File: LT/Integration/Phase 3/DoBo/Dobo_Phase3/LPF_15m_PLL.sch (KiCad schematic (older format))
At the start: 11 parts, among them J300 Conn_Coaxial, J301 Conn_Coaxial

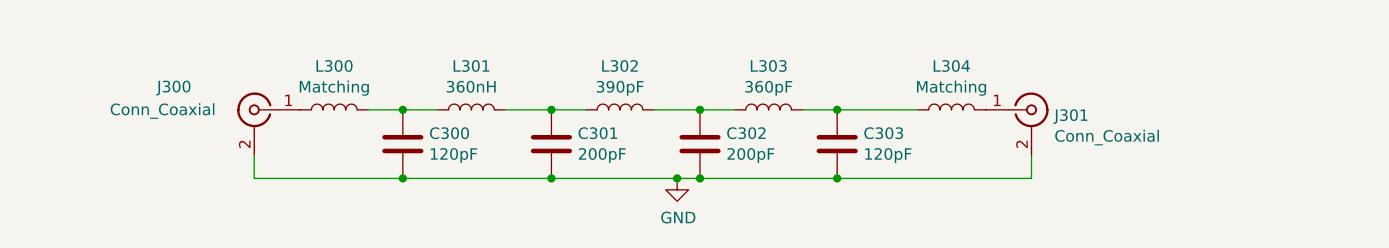
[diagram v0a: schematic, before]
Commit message: Added the completed layout for the DoBo Phase 3
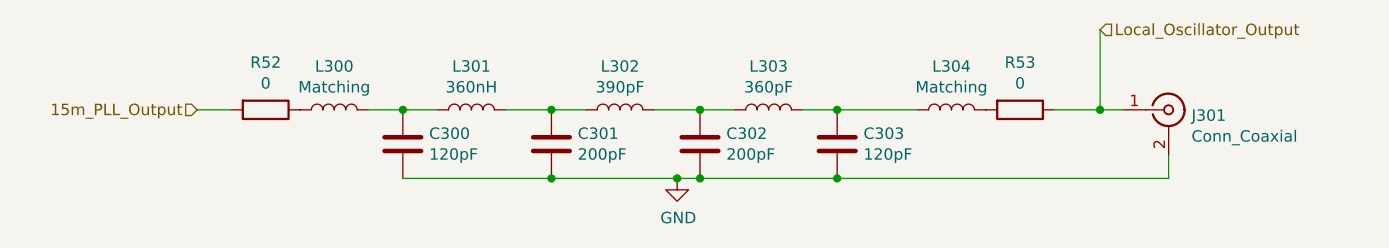
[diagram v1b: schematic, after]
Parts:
- removed J300: Conn_Coaxial, Connector_Coaxial:SMA_Amphenol_132289_EdgeMount, symbol Connector:Conn_Coaxial
- added R52, R53: 0, Resistor_SMD:R_0805_2012Metric_Pad1.15x1.40mm_HandSolder, symbol Device:R
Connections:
- net at L300.1: now also R52.1
- net at L304.2: now also R53.2; no longer J301.1 (In)
- new net 15m_PLL_Output: R52.2
- new net Local_Oscillator_Output: J301.1 (In), R53.1
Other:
- moved on the sheet: J301
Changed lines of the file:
@@
 $Descr A4 11693 8268
 encoding utf-8
-Sheet 9 10
+Sheet 6 10
 Title ""
 Date ""
@@
 $EndDescr
 $Comp
-L Connector:Conn_Coaxial J300
-U 1 1 5E4DB0EF
-P 2850 2200
-F 0 "J300" H 3200 2300 50  0000 C CNN
-F 1 "Conn_Coaxial" H 3250 2200 50  0000 C CNN
-F 2 "Connector_Coaxial:SMA_Amphenol_132289_EdgeMount" H 2850 2200 50  0001 C CNN
-F 3 " ~" H 2850 2200 50  0001 C CNN
-	1    2850 2200
-	-1   0    0    -1
-$EndComp
-$Comp
 L Device:L L301
 U 1 1 5E4DF0E6
@@
 L Connector:Conn_Coaxial J301
 U 1 1 5E4E4646
-P 6250 2200
-F 0 "J301" H 6350 2175 50  0000 L CNN
-F 1 "Conn_Coaxial" H 6350 2084 50  0000 L CNN
-F 2 "Connector_Coaxial:SMA_Amphenol_132289_EdgeMount" H 6250 2200 50  0001 C CNN
-F 3 " ~" H 6250 2200 50  0001 C CNN
-	1    6250 2200
+P 6850 2200
+F 0 "J301" H 6950 2175 50  0000 L CNN
+F 1 "Conn_Coaxial" H 6950 2084 50  0000 L CNN
+F 2 "Connector_Coaxial:SMA_Amphenol_132289_EdgeMount" H 6850 2200 50  0001 C CNN
+F 3 " ~" H 6850 2200 50  0001 C CNN
+	1    6850 2200
 	1    0    0    -1
 $EndComp
@@
 Wire Wire Line
 	5400 2200 5750 2200
-Connection ~ 3500 2500
 Wire Wire Line
 	3500 2500 4150 2500
@@
 Wire Wire Line
 	4800 2500 5400 2500
-Connection ~ 5400 2500
 $Comp
 L Device:L L300
@@
 $EndComp
 Wire Wire Line
-	2850 2400 2850 2500
-Wire Wire Line
-	2850 2500 3500 2500
-Wire Wire Line
-	6250 2500 6250 2400
-Wire Wire Line
-	5400 2500 6250 2500
+	6850 2500 6850 2400
 $Comp
 L power:GND #PWR0129
@@
 Wire Wire Line
 	4700 2500 4800 2500
+$Comp
+L Device:R R52
+U 1 1 5EE2561E
+P 2900 2200
+F 0 "R52" V 2693 2200 50  0000 C CNN
+F 1 "0" V 2784 2200 50  0000 C CNN
+F 2 "Resistor_SMD:R_0805_2012Metric_Pad1.15x1.40mm_HandSolder" V 2830 2200 50  0001 C CNN
+F 3 "~" H 2900 2200 50  0001 C CNN
+	1    2900 2200
+	0    1    1    0
+$EndComp
+Text HLabel 2600 2200 0    50   Input ~ 0
+15m_PLL_Output
+Wire Wire Line
+	2600 2200 2750 2200
+$Comp
+L Device:R R53
+U 1 1 5EE26D32
+P 6200 2200
+F 0 "R53" V 5993 2200 50  0000 C CNN
+F 1 "0" V 6084 2200 50  0000 C CNN
+F 2 "Resistor_SMD:R_0805_2012Metric_Pad1.15x1.40mm_HandSolder" V 6130 2200 50  0001 C CNN
+F 3 "~" H 6200 2200 50  0001 C CNN
+	1    6200 2200
+	0    1    1    0
+$EndComp
+Text HLabel 6550 1850 2    50   Input ~ 0
+Local_Oscillator_Output
+Wire Wire Line
+	5400 2500 6850 2500
+Connection ~ 5400 2500
+Wire Wire Line
+	6350 2200 6550 2200
+Wire Wire Line
+	6550 1850 6550 2200
+Connection ~ 6550 2200
+Wire Wire Line
+	6550 2200 6650 2200
 $EndSCHEMATC

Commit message: Adding the DoBo Phase 3 integration with all traces routed
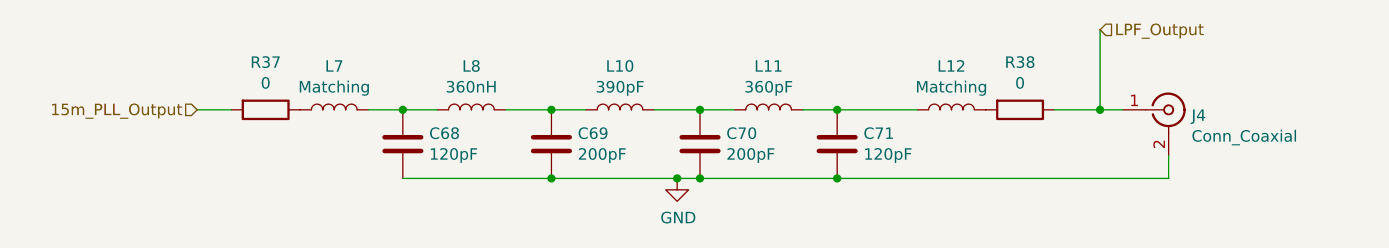
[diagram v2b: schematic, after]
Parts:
- renumbered C300 to C68, C301 to C69, C302 to C70, C303 to C71, J301 to J4, L302 to L10, L303 to L11, L304 to L12, L300 to L7, L301 to L8, R52 to R37, R53 to R38
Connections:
- net Local_Oscillator_Output renamed LPF_Output
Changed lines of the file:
@@
 $Descr A4 11693 8268
 encoding utf-8
-Sheet 6 10
+Sheet 5 10
 Title ""
 Date ""
@@
 $EndDescr
 $Comp
-L Device:L L301
+L Device:L L8
 U 1 1 5E4DF0E6
 P 3800 2200
-F 0 "L301" V 3990 2200 50  0000 C CNN
+F 0 "L8" V 3990 2200 50  0000 C CNN
 F 1 "360nH" V 3899 2200 50  0000 C CNN
 F 2 "Inductor_SMD:L_0402_1005Metric" H 3800 2200 50  0001 C CNN
@@
 $EndComp
 $Comp
-L Device:C C300
+L Device:C C68
 U 1 1 5E4E04B0
 P 3500 2350
-F 0 "C300" H 3615 2396 50  0000 L CNN
+F 0 "C68" H 3615 2396 50  0000 L CNN
 F 1 "120pF" H 3615 2305 50  0000 L CNN
 F 2 "Capacitor_SMD:C_0402_1005Metric" H 3538 2200 50  0001 C CNN
@@
 $EndComp
 $Comp
-L Device:L L302
+L Device:L L10
 U 1 1 5E4E2C92
 P 4450 2200
-F 0 "L302" V 4640 2200 50  0000 C CNN
+F 0 "L10" V 4640 2200 50  0000 C CNN
 F 1 "390pF" V 4549 2200 50  0000 C CNN
 F 2 "Inductor_SMD:L_0402_1005Metric" H 4450 2200 50  0001 C CNN
@@
 $EndComp
 $Comp
-L Device:C C301
+L Device:C C69
 U 1 1 5E4E2C98
 P 4150 2350
-F 0 "C301" H 4265 2396 50  0000 L CNN
+F 0 "C69" H 4265 2396 50  0000 L CNN
 F 1 "200pF" H 4265 2305 50  0000 L CNN
 F 2 "Capacitor_SMD:C_0402_1005Metric" H 4188 2200 50  0001 C CNN
@@
 $EndComp
 $Comp
-L Device:L L303
+L Device:L L11
 U 1 1 5E4E342C
 P 5100 2200
-F 0 "L303" V 5290 2200 50  0000 C CNN
+F 0 "L11" V 5290 2200 50  0000 C CNN
 F 1 "360pF" V 5199 2200 50  0000 C CNN
 F 2 "Inductor_SMD:L_0402_1005Metric" H 5100 2200 50  0001 C CNN
@@
 $EndComp
 $Comp
-L Device:C C302
+L Device:C C70
 U 1 1 5E4E3432
 P 4800 2350
-F 0 "C302" H 4915 2396 50  0000 L CNN
+F 0 "C70" H 4915 2396 50  0000 L CNN
 F 1 "200pF" H 4915 2305 50  0000 L CNN
 F 2 "Capacitor_SMD:C_0402_1005Metric" H 4838 2200 50  0001 C CNN
@@
 $EndComp
 $Comp
-L Device:C C303
+L Device:C C71
 U 1 1 5E4E4116
 P 5400 2350
-F 0 "C303" H 5515 2396 50  0000 L CNN
+F 0 "C71" H 5515 2396 50  0000 L CNN
 F 1 "120pF" H 5515 2305 50  0000 L CNN
 F 2 "Capacitor_SMD:C_0402_1005Metric" H 5438 2200 50  0001 C CNN
@@
 $EndComp
 $Comp
-L Connector:Conn_Coaxial J301
+L Connector:Conn_Coaxial J4
 U 1 1 5E4E4646
 P 6850 2200
-F 0 "J301" H 6950 2175 50  0000 L CNN
+F 0 "J4" H 6950 2175 50  0000 L CNN
 F 1 "Conn_Coaxial" H 6950 2084 50  0000 L CNN
 F 2 "Connector_Coaxial:SMA_Amphenol_132289_EdgeMount" H 6850 2200 50  0001 C CNN
@@
 	4800 2500 5400 2500
 $Comp
-L Device:L L300
+L Device:L L7
 U 1 1 5E4E763A
 P 3200 2200
-F 0 "L300" V 3390 2200 50  0000 C CNN
+F 0 "L7" V 3390 2200 50  0000 C CNN
 F 1 "Matching" V 3299 2200 50  0000 C CNN
 F 2 "Inductor_SMD:L_0402_1005Metric" H 3200 2200 50  0001 C CNN
@@
 $EndComp
 $Comp
-L Device:L L304
+L Device:L L12
 U 1 1 5E4E8526
 P 5900 2200
-F 0 "L304" V 6090 2200 50  0000 C CNN
+F 0 "L12" V 6090 2200 50  0000 C CNN
 F 1 "Matching" V 5999 2200 50  0000 C CNN
 F 2 "Inductor_SMD:L_0402_1005Metric" H 5900 2200 50  0001 C CNN
@@
 	6850 2500 6850 2400
 $Comp
-L power:GND #PWR0129
+L power:GND #PWR0144
 U 1 1 5E4E98C9
 P 4700 2500
-F 0 "#PWR0129" H 4700 2250 50  0001 C CNN
+F 0 "#PWR0144" H 4700 2250 50  0001 C CNN
 F 1 "GND" H 4705 2327 50  0000 C CNN
 F 2 "" H 4700 2500 50  0001 C CNN
@@
 	4700 2500 4800 2500
 $Comp
-L Device:R R52
+L Device:R R37
 U 1 1 5EE2561E
 P 2900 2200
-F 0 "R52" V 2693 2200 50  0000 C CNN
+F 0 "R37" V 2693 2200 50  0000 C CNN
 F 1 "0" V 2784 2200 50  0000 C CNN
 F 2 "Resistor_SMD:R_0805_2012Metric_Pad1.15x1.40mm_HandSolder" V 2830 2200 50  0001 C CNN
@@
 	2600 2200 2750 2200
 $Comp
-L Device:R R53
+L Device:R R38
 U 1 1 5EE26D32
 P 6200 2200
-F 0 "R53" V 5993 2200 50  0000 C CNN
+F 0 "R38" V 5993 2200 50  0000 C CNN
 F 1 "0" V 6084 2200 50  0000 C CNN
 F 2 "Resistor_SMD:R_0805_2012Metric_Pad1.15x1.40mm_HandSolder" V 6130 2200 50  0001 C CNN
@@
 $EndComp
 Text HLabel 6550 1850 2    50   Input ~ 0
-Local_Oscillator_Output
+LPF_Output
 Wire Wire Line
 	5400 2500 6850 2500
